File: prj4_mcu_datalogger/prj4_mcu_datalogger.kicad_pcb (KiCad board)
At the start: 2 copper layers, 53.3 x 34.9 mm, 31 parts, among them J1 Conn_01x04_Pin, J2 Conn_01x04_Pin, J3 Conn_01x09_Pin, J4 Conn_02x03_Odd_Even, U1 DS1337S+, U2 ATMEGA328P-AU, U3 24LC1025, U4 24LC1025, Y1 32.768 KHz, Y2 16 MHz

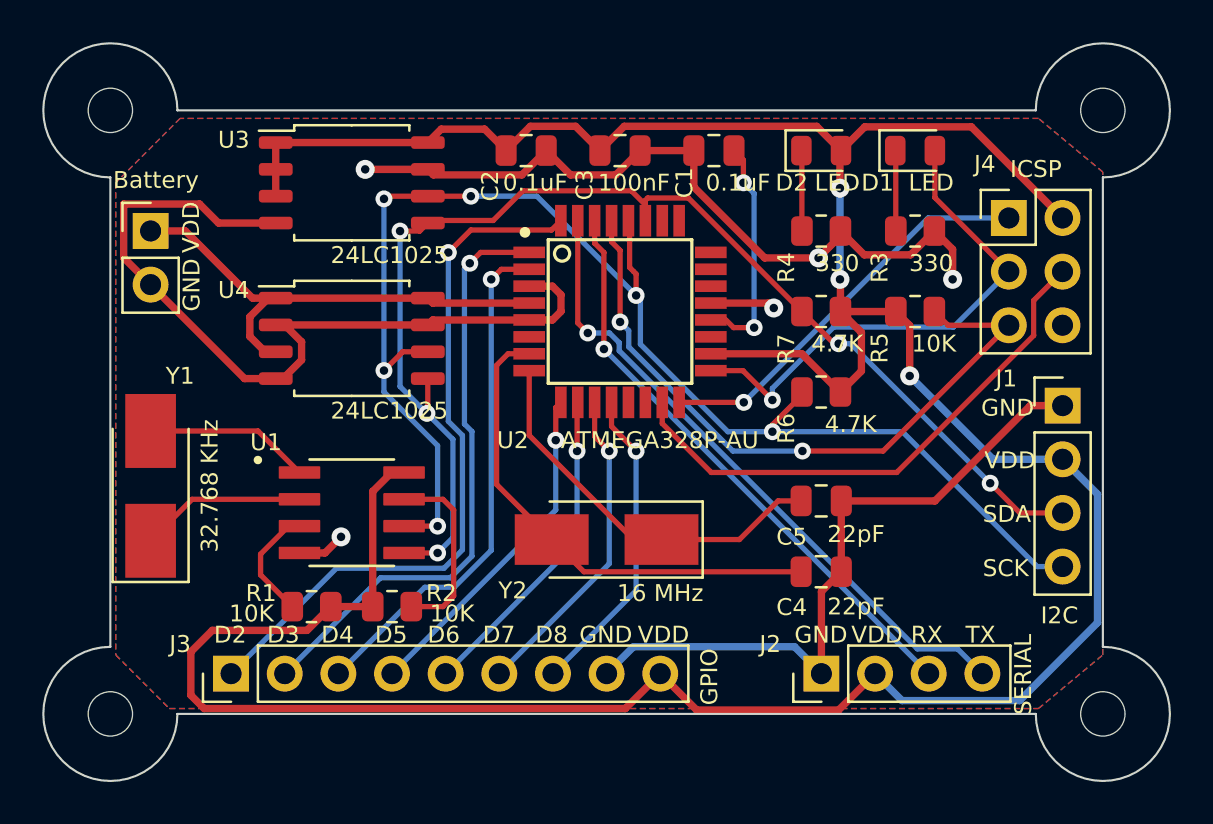
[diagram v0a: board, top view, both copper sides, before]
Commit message: Completate le connessioni tra i componenti del PCB
Feat: connessi i vari componenti del PCB
Feat: effettuato DRC per verificare correttezza
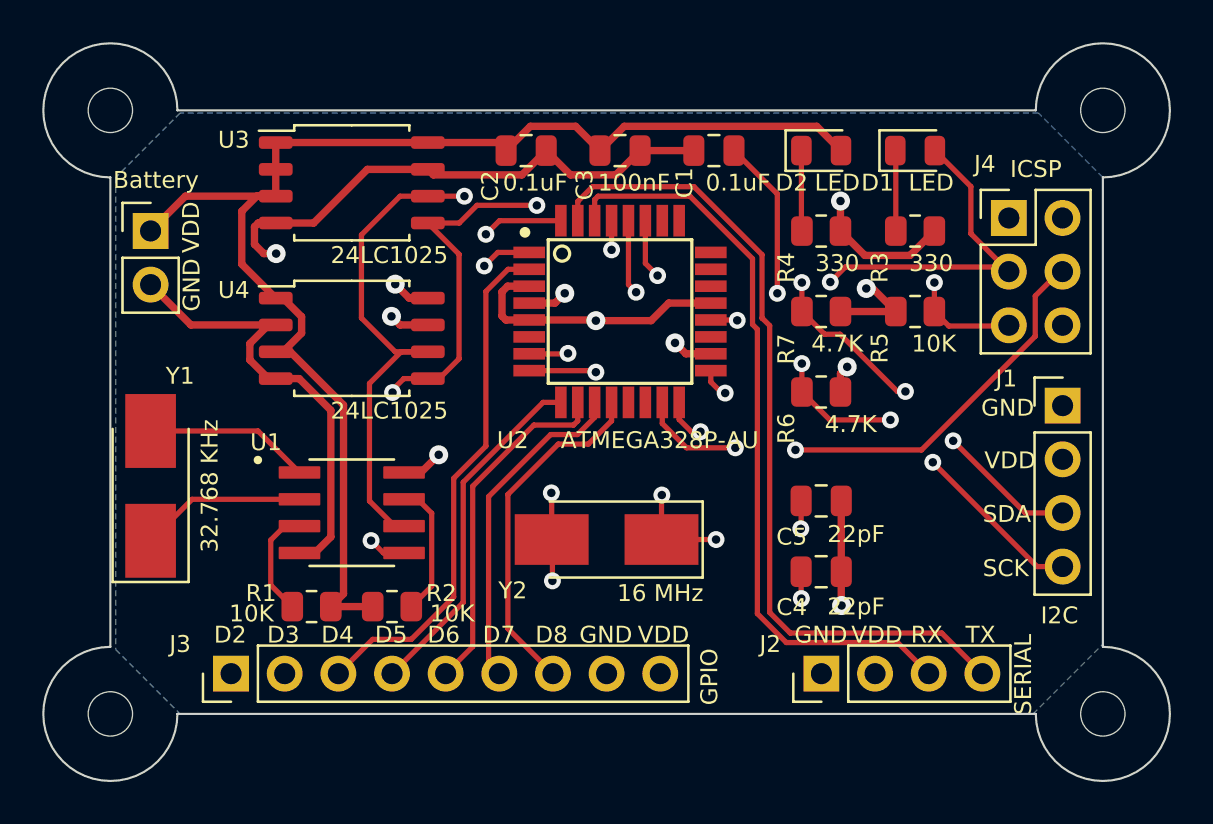
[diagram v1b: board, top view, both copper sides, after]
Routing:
- net /Vcc: track 176.6 -> 78.0 mm, vias 3 -> 6
- net GND: track 113.5 -> 73.7 mm
- net /RESET: track 32.6 -> 22.5 mm
- net /TX: track 31.1 -> 39.6 mm, vias 1 -> 0
- net /RX: track 28.0 -> 36.0 mm, vias 1 -> 0
- net /MISO: track 19.2 -> 22.9 mm
- net Net-(U2-PB6): track 23.5 -> 27.1 mm, vias 0 -> 4
- net /SCL: track 67.4 -> 64.4 mm, vias 6 -> 5
- net Net-(U1-SQW/~INT): track 8.84 -> 6.40 mm
- net /SCK: track 24.7 -> 26.8 mm, vias 1 -> 2
- net Net-(U2-PB7): track 18.7 -> 20.5 mm, vias 0 -> 4
- net /D8: track 15.0 -> 16.6 mm, vias 1 -> 0
- net /D2: track 33.7 -> 32.1 mm
- net /D3: track 28.3 -> 26.9 mm
- net /D6: track 15.4 -> 16.5 mm, vias 1 -> 0
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- added copper zone on In2.Cu, net /Vcc
- removed copper zone on F.Cu, net /Vcc
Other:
- copper layers 2 -> 4

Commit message: Aggiunte informazioni - progetto completato
Feat: aggiunte informazioni sul PCB
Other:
- board text added: "4"
- board text removed: "2"
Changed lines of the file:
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@@
     (effects (font (size 0.8 0.8) (thickness 0.15)) (justify left bottom))
   )
-  (gr_text "" (at 166.573481 128.0182) (layer "User.3")
-    (effects (font (size 1.5 1.5) (thickness 0.2)) (justify left top))
-  )
-  (gr_text "1,6000 mm" (at 191.516338 124.0612) (layer "User.3")
-    (effects (font (size 1.5 1.5) (thickness 0.2)) (justify left top))
-  )
-  (gr_text "BOARD CHARACTERISTICS" (at 99.0092 118.5672) (layer "User.3")
+  (gr_text "Min hole diameter: " (at 166.700481 131.645) (layer "User.3")
+    (effects (font (size 1.5 1.5) (thickness 0.2)) (justify left top))
+  )
+  (gr_text "4" (at 132.543343 123.731) (layer "User.3")
+    (effects (font (size 1.5 1.5) (thickness 0.2)) (justify left top))
+  )
+  (gr_text "BOARD CHARACTERISTICS" (at 99.1362 118.237) (layer "User.3")
     (effects (font (size 2 2) (thickness 0.4)) (justify left top))
   )
-  (gr_text "None" (at 132.416343 135.9322) (layer "User.3")
-    (effects (font (size 1.5 1.5) (thickness 0.2)) (justify left top))
-  )
-  (gr_text "Castellated pads: " (at 99.7592 139.8892) (layer "User.3")
-    (effects (font (size 1.5 1.5) (thickness 0.2)) (justify left top))
-  )
-  (gr_text "2" (at 132.416343 124.0612) (layer "User.3")
-    (effects (font (size 1.5 1.5) (thickness 0.2)) (justify left top))
-  )
-  (gr_text "Min track/spacing: " (at 99.7592 131.9752) (layer "User.3")
-    (effects (font (size 1.5 1.5) (thickness 0.2)) (justify left top))
-  )
-  (gr_text "No" (at 191.516338 135.9322) (layer "User.3")
-    (effects (font (size 1.5 1.5) (thickness 0.2)) (justify left top))
-  )
-  (gr_text "Edge card connectors: " (at 99.7592 143.8462) (layer "User.3")
-    (effects (font (size 1.5 1.5) (thickness 0.2)) (justify left top))
-  )
-  (gr_text "0,3000 mm" (at 191.516338 131.9752) (layer "User.3")
-    (effects (font (size 1.5 1.5) (thickness 0.2)) (justify left top))
-  )
-  (gr_text "Plated Board Edge: " (at 166.573481 139.8892) (layer "User.3")
-    (effects (font (size 1.5 1.5) (thickness 0.2)) (justify left top))
-  )
-  (gr_text "Board overall dimensions: " (at 99.7592 128.0182) (layer "User.3")
-    (effects (font (size 1.5 1.5) (thickness 0.2)) (justify left top))
-  )
-  (gr_text "Board Thickness: " (at 166.573481 124.0612) (layer "User.3")
-    (effects (font (size 1.5 1.5) (thickness 0.2)) (justify left top))
-  )
-  (gr_text "53,3400 mm x 34,9250 mm" (at 132.416343 128.0182) (layer "User.3")
-    (effects (font (size 1.5 1.5) (thickness 0.2)) (justify left top))
-  )
-  (gr_text "No" (at 191.516338 139.8892) (layer "User.3")
-    (effects (font (size 1.5 1.5) (thickness 0.2)) (justify left top))
-  )
-  (gr_text "Min hole diameter: " (at 166.573481 131.9752) (layer "User.3")
-    (effects (font (size 1.5 1.5) (thickness 0.2)) (justify left top))
-  )
-  (gr_text "No" (at 132.416343 139.8892) (layer "User.3")
-    (effects (font (size 1.5 1.5) (thickness 0.2)) (justify left top))
-  )
-  (gr_text "No" (at 132.416343 143.8462) (layer "User.3")
-    (effects (font (size 1.5 1.5) (thickness 0.2)) (justify left top))
-  )
-  (gr_text "" (at 191.516338 128.0182) (layer "User.3")
-    (effects (font (size 1.5 1.5) (thickness 0.2)) (justify left top))
-  )
-  (gr_text "Copper Layer Count: " (at 99.7592 124.0612) (layer "User.3")
-    (effects (font (size 1.5 1.5) (thickness 0.2)) (justify left top))
-  )
-  (gr_text "0,2000 mm / 0,0000 mm" (at 132.416343 131.9752) (layer "User.3")
-    (effects (font (size 1.5 1.5) (thickness 0.2)) (justify left top))
-  )
-  (gr_text "Copper Finish: " (at 99.7592 135.9322) (layer "User.3")
-    (effects (font (size 1.5 1.5) (thickness 0.2)) (justify left top))
-  )
-  (gr_text "Impedance Control: " (at 166.573481 135.9322) (layer "User.3")
+  (gr_text "Copper Finish: " (at 99.8862 135.602) (layer "User.3")
+    (effects (font (size 1.5 1.5) (thickness 0.2)) (justify left top))
+  )
+  (gr_text "No" (at 132.543343 139.559) (layer "User.3")
+    (effects (font (size 1.5 1.5) (thickness 0.2)) (justify left top))
+  )
+  (gr_text "Board overall dimensions: " (at 99.8862 127.688) (layer "User.3")
+    (effects (font (size 1.5 1.5) (thickness 0.2)) (justify left top))
+  )
+  (gr_text "No" (at 191.643338 139.559) (layer "User.3")
+    (effects (font (size 1.5 1.5) (thickness 0.2)) (justify left top))
+  )
+  (gr_text "1,6000 mm" (at 191.643338 123.731) (layer "User.3")
+    (effects (font (size 1.5 1.5) (thickness 0.2)) (justify left top))
+  )
+  (gr_text "None" (at 132.543343 135.602) (layer "User.3")
+    (effects (font (size 1.5 1.5) (thickness 0.2)) (justify left top))
+  )
+  (gr_text "Plated Board Edge: " (at 166.700481 139.559) (layer "User.3")
+    (effects (font (size 1.5 1.5) (thickness 0.2)) (justify left top))
+  )
+  (gr_text "No" (at 191.643338 135.602) (layer "User.3")
+    (effects (font (size 1.5 1.5) (thickness 0.2)) (justify left top))
+  )
+  (gr_text "Min track/spacing: " (at 99.8862 131.645) (layer "User.3")
+    (effects (font (size 1.5 1.5) (thickness 0.2)) (justify left top))
+  )
+  (gr_text "No" (at 132.543343 143.516) (layer "User.3")
+    (effects (font (size 1.5 1.5) (thickness 0.2)) (justify left top))
+  )
+  (gr_text "Copper Layer Count: " (at 99.8862 123.731) (layer "User.3")
+    (effects (font (size 1.5 1.5) (thickness 0.2)) (justify left top))
+  )
+  (gr_text "0,3000 mm" (at 191.643338 131.645) (layer "User.3")
+    (effects (font (size 1.5 1.5) (thickness 0.2)) (justify left top))
+  )
+  (gr_text "Impedance Control: " (at 166.700481 135.602) (layer "User.3")
+    (effects (font (size 1.5 1.5) (thickness 0.2)) (justify left top))
+  )
+  (gr_text "0,2000 mm / 0,0000 mm" (at 132.543343 131.645) (layer "User.3")
+    (effects (font (size 1.5 1.5) (thickness 0.2)) (justify left top))
+  )
+  (gr_text "53,3400 mm x 34,9250 mm" (at 132.543343 127.688) (layer "User.3")
+    (effects (font (size 1.5 1.5) (thickness 0.2)) (justify left top))
+  )
+  (gr_text "" (at 166.700481 127.688) (layer "User.3")
+    (effects (font (size 1.5 1.5) (thickness 0.2)) (justify left top))
+  )
+  (gr_text "Castellated pads: " (at 99.8862 139.559) (layer "User.3")
+    (effects (font (size 1.5 1.5) (thickness 0.2)) (justify left top))
+  )
+  (gr_text "Board Thickness: " (at 166.700481 123.731) (layer "User.3")
+    (effects (font (size 1.5 1.5) (thickness 0.2)) (justify left top))
+  )
+  (gr_text "" (at 191.643338 127.688) (layer "User.3")
+    (effects (font (size 1.5 1.5) (thickness 0.2)) (justify left top))
+  )
+  (gr_text "Edge card connectors: " (at 99.8862 143.516) (layer "User.3")
     (effects (font (size 1.5 1.5) (thickness 0.2)) (justify left top))
   )
@@
     )
   )
-  (group "group-boardCharacteristics" (id 48a9f634-1ed8-4863-b72a-47090ae65aaf)
+  (group "group-boardCharacteristics" (id 835a4985-3e47-4add-b795-97bb868c2b42)
     (members
-      016b7c7d-808c-4f24-af57-e0aaa92c5276
-      0815367c-585e-4733-8b6e-43b165b97ba8
-      1e3ecf31-6488-4c28-bf2f-e8f0c557f147
-      1ffa4aaa-3449-4395-bf45-7b8def4fe71e
-      2be232a7-b6d6-4bcf-bfe9-01282eeb2469
-      30a7f5fb-defe-482c-85a5-ed5333db6d84
-      4406447b-1fb6-4948-9ccd-133cf06ad0aa
-      4480ad8a-d0c6-44ab-8487-528564bb272a
-      4d6738fc-ba97-43a1-b47c-3ad8bbe08d26
-      5fc2906a-25e2-483f-8bde-0476cdd31fe0
-      7e0ce513-16d4-4113-9c54-80082688610d
-      88e53aee-dba3-4ada-87b6-c0382b93037e
-      8f98d622-b351-4b3f-b190-d4621321c43d
-      aa829264-62ff-43fc-9f48-d0129898dc27
-      b4a7c9b9-c3c4-4d16-a345-8938557b2338
-      b6fb1491-6c38-4ccc-94ce-1f5fdafc045a
-      b745a141-6a2b-4fe2-9a92-bbd22cc450b7
-      bda995ab-5720-48e8-b34c-f51b8063a754
-      be58cea6-572c-4740-9f2f-0cfed18a746f
-      d261df76-362a-42f7-9c8a-9b27b2a2a0e2
-      d7f85d98-6fbf-4672-931d-c95a39241ce7
-      e92aa405-69c0-4992-ae06-e79158359de9
-      f330ad66-3fc5-4acb-896b-409801432205
+      123ae61d-e14e-48c0-a285-b501f646d67b
+      23c508bf-f5be-4024-9732-a325f46190ce
+      3cfe7adf-70c3-4f37-bc22-ede9b40fa5b3
+      4b7cca96-bfdf-45c3-bcb8-402361f4100e
+      4d347414-da70-487a-a129-9c17587dad51
+      5de5d3f2-62de-4ed3-ad85-be648da4f9fd
+      63a4399e-a40d-4377-8f06-366acc4e96a0
+      67663d47-6616-48a6-a25e-65ee57d5cdcd
+      6afa1b57-df0d-450a-ae1d-79cc885d5748
+      76828ecb-5a7d-4863-957e-7344b6b51470
+      8ac9e2f8-e632-479f-9dfb-94bd66abc007
+      8f70d793-0f4f-4668-b867-0858f1773674
+      9dedd8d1-f0d1-422f-8ee2-7ad8fa5b4681
+      aa90b51b-3cb2-493e-b639-b32025578558
+      b6dc6260-4f9a-4da5-a48f-d82862f38ed8
+      c167c3d5-b9c6-4978-858b-9d02707604f4
+      c3a206e5-2bca-45a2-b823-1bd8090e9281
+      d49a92cf-a450-48d8-92aa-2c011b700e9c
+      d757f406-a52f-465e-8f14-a837fa7cd1a4
+      d75b7921-1dbc-43d7-b69f-3984128a7014
+      d84e868c-4c9f-4918-906c-3ab9034df781
+      d9ed89d3-54ac-4df1-914c-35a7474b2c3d
+      f4218f24-52e9-4e82-8479-ed02a38b5624
     )
   )

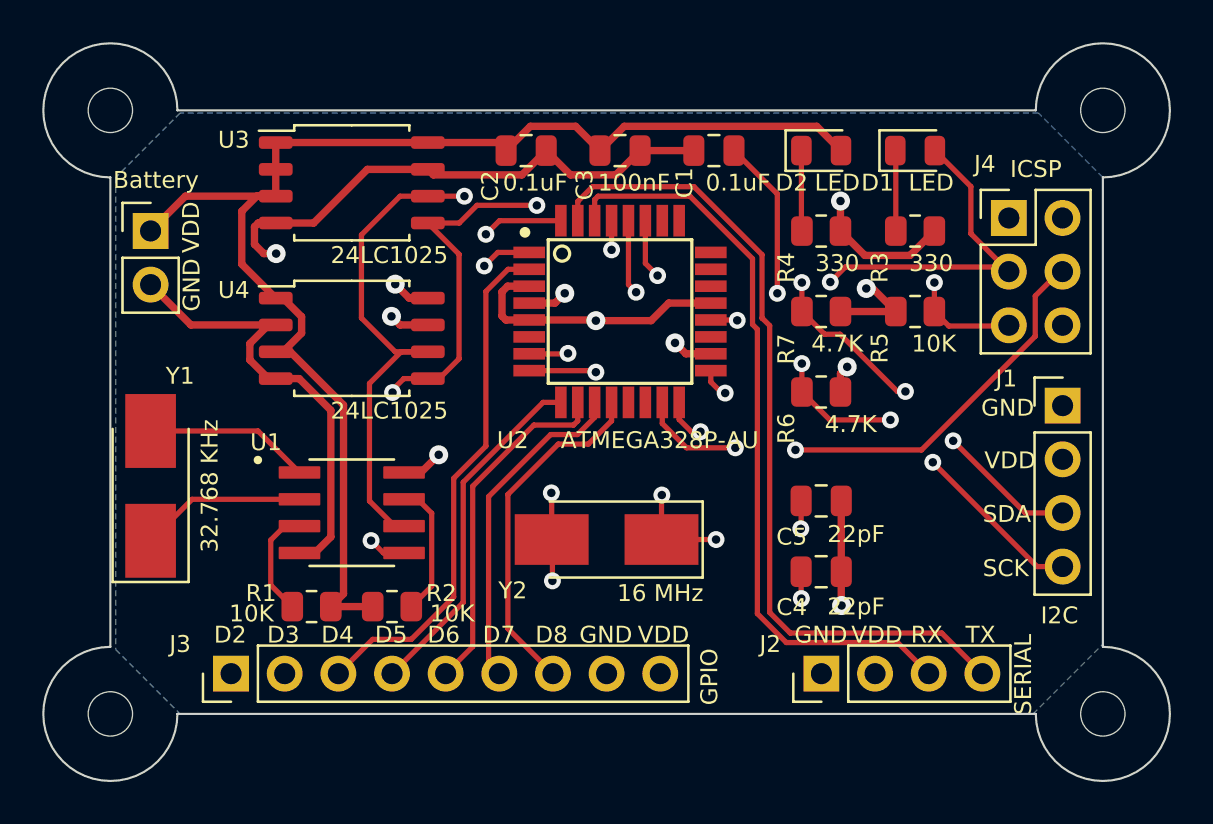
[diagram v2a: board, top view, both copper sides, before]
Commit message: Rimosse tutte le connessioni tra i componenti
Feat: eliminate tracce e via
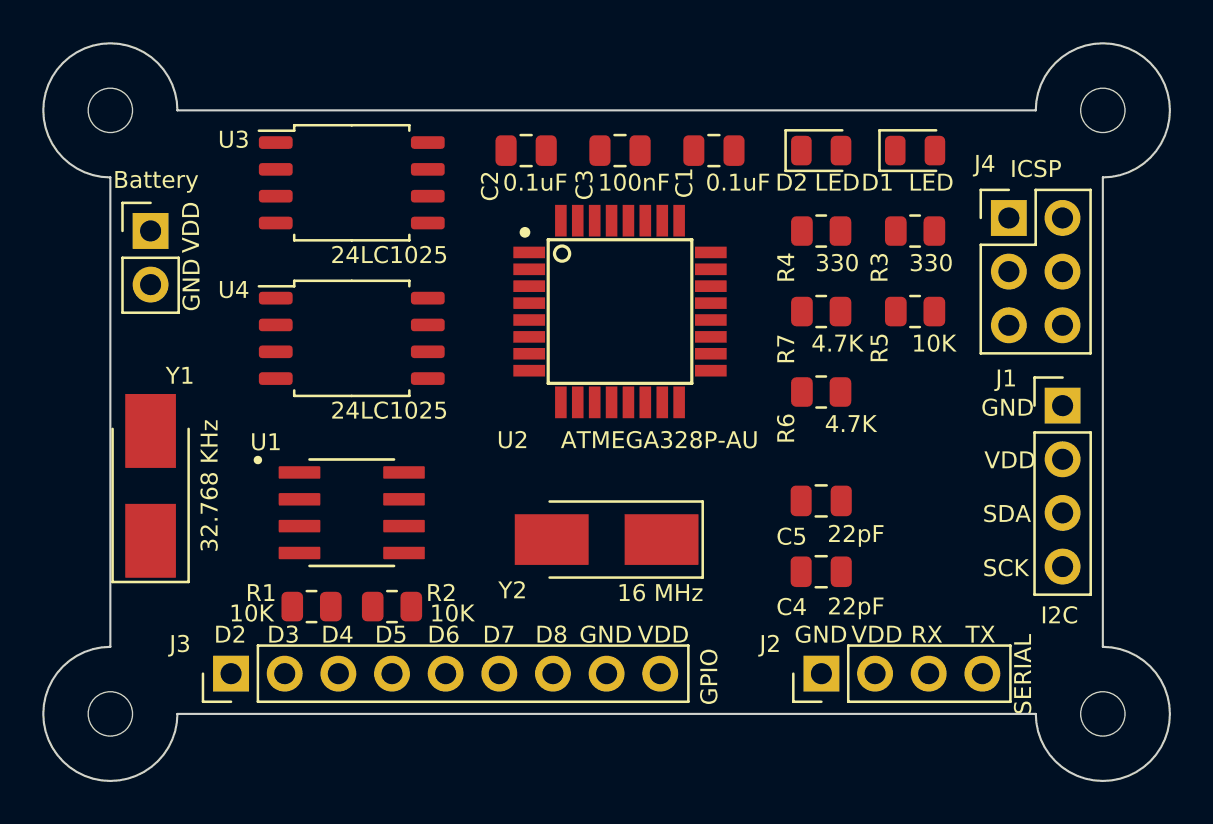
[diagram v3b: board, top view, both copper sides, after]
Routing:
- net /Vcc: track 78.0 -> 0.00 mm, vias 6 -> 0
- net GND: track 73.7 -> 0.00 mm, vias 5 -> 0
- net /SCL: track 64.4 -> 0.00 mm, vias 5 -> 0
- net /SDA: track 60.6 -> 0.00 mm, vias 7 -> 0
- net /TX: track 39.6 -> 0.00 mm
- net /RX: track 36.0 -> 0.00 mm
- net /D2: track 32.1 -> 0.00 mm, vias 1 -> 0
- net Net-(U2-PB6): track 27.1 -> 0.00 mm, vias 4 -> 0
- net /D3: track 26.9 -> 0.00 mm, vias 1 -> 0
- net /SCK: track 26.8 -> 0.00 mm, vias 2 -> 0
- net /MOSI: track 25.1 -> 0.00 mm, vias 2 -> 0
- net /D4: track 24.5 -> 0.00 mm
- net /MISO: track 22.9 -> 0.00 mm, vias 1 -> 0
- net /RESET: track 22.5 -> 0.00 mm, vias 2 -> 0
- net Net-(U2-PB7): track 20.5 -> 0.00 mm, vias 4 -> 0
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- removed copper zone on In2.Cu, net /Vcc
- removed copper zone on B.Cu, net GND

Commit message: Create connessioni mediante Freerouting
Feat: creato routing automatico
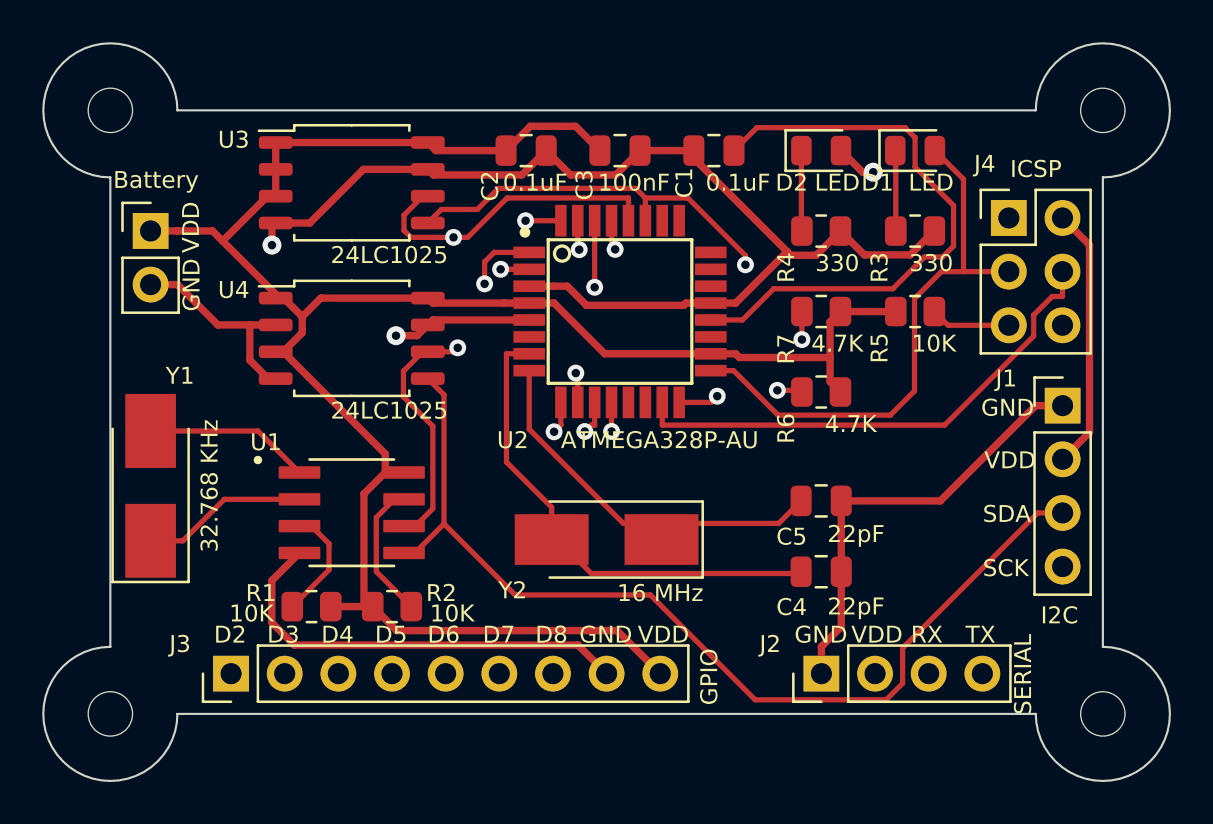
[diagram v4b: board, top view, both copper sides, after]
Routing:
- net GND: track 0.00 -> 159.4 mm, vias 0 -> 2
- net /Vcc: track 0.00 -> 149.5 mm, vias 0 -> 1
- net /SDA: track 0.00 -> 87.3 mm, vias 0 -> 2
- net /SCL: track 0.00 -> 66.1 mm, vias 0 -> 3
- net /TX: track 0.00 -> 30.1 mm, vias 0 -> 1
- net /D2: track 0.00 -> 28.9 mm, vias 0 -> 1
- net Net-(U2-AREF): track 0.00 -> 28.0 mm
- net /RX: track 0.00 -> 28.0 mm, vias 0 -> 1
- net /SCK: track 0.00 -> 26.7 mm
- net /D3: track 0.00 -> 25.7 mm, vias 0 -> 1
- net /RESET: track 0.00 -> 25.4 mm, vias 0 -> 1
- net /MOSI: track 0.00 -> 24.3 mm
- net /D4: track 0.00 -> 23.7 mm, vias 0 -> 1
- net Net-(U2-PB6): track 0.00 -> 23.4 mm
- net /MISO: track 0.00 -> 19.2 mm, vias 0 -> 1
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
